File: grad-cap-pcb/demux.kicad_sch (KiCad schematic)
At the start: 0 parts

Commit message: addd more
switched from npn to pnp to make the LEDs connect to the ground plane - easier routing.
added labels and or gates so the mosfets wouldnt trigger each other
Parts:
- added R1, R2, R3: 0 ohms, Resistor_SMD:R_0603_1608Metric, symbol Device:R_Small_US
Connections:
- new net: R1.1, R2.1

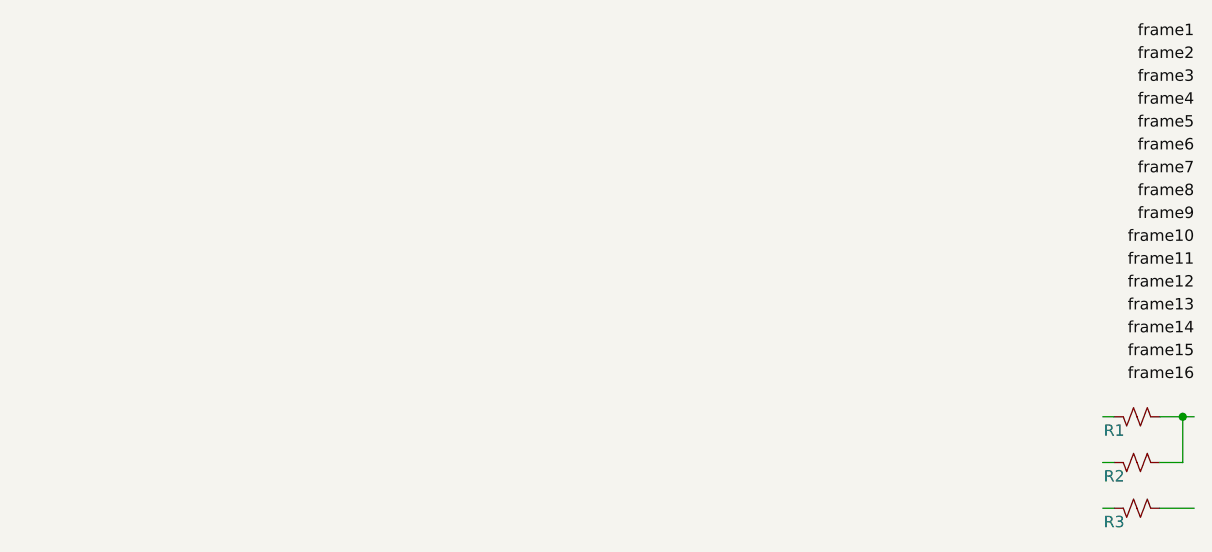
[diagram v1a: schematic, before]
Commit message: added many things
added: mux
counter
signal gen - still needs r1 and r2 values
power management
kicad symbol library - footprints not assigned
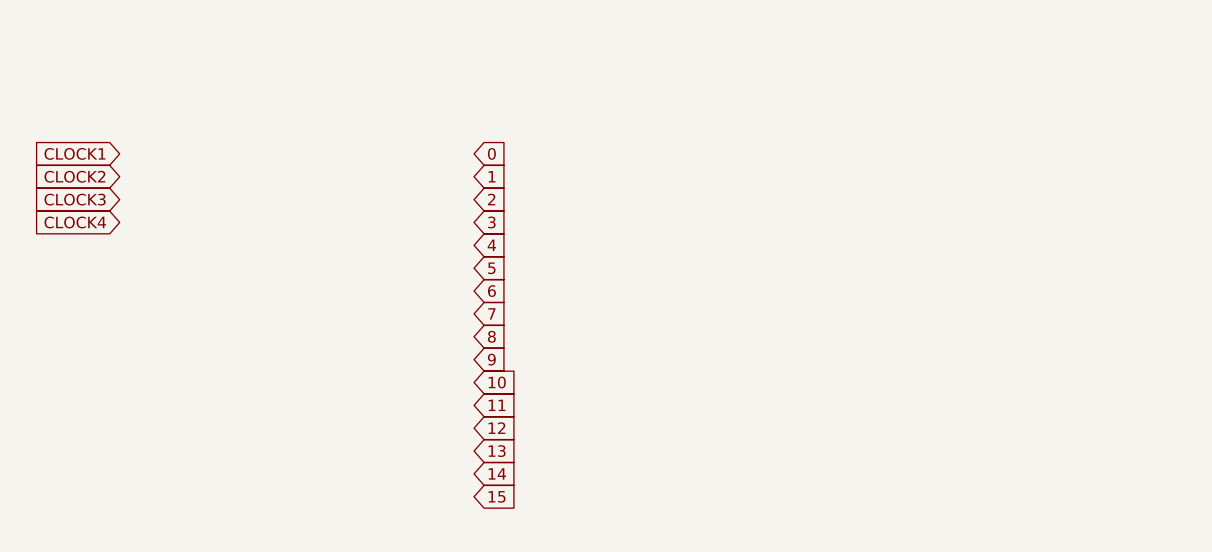
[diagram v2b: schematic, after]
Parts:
- removed R1, R2, R3: 0 ohms, Resistor_SMD:R_0603_1608Metric, symbol Device:R_Small_US
